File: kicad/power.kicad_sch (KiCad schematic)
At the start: 10 parts, among them Q1 DMN62D0UW-7, U14 TC2117-3.3VDBTR

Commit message: checking shunt footprints
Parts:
- added C53, C54: 220uF 63V, footprints:CHEMI-KG5, symbol Device:C_Polarized
- added C57: 100uF 63V, Capacitor_SMD:CP_Elec_8x10.5, symbol Device:C_Polarized
- C55: renamed from C51; value 470uF 63V -> 100uF 63V; footprint Capacitor_SMD:CP_Elec_16x17.5 -> Capacitor_SMD:CP_Elec_8x10.5
- C56: renamed from C52; value 470uF 63V -> 100uF 63V; footprint Capacitor_SMD:CP_Elec_16x17.5 -> Capacitor_SMD:CP_Elec_8x10.5
- renumbered C53 to C58, C54 to C59, C55 to C60, D2 to D9, Q1 to Q7, R7 to R43, R6 to R44
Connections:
- net GND: now also C53.2, C54.2, C57.2
- net SUPPLY: now also C53.1, C54.1, C57.1
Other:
- moved on the sheet: C55, C56

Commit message: routing gate driver
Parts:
- removed C55, C56, C57: 100uF 63V, Capacitor_SMD:CP_Elec_8x10.5, symbol Device:C_Polarized
- C53, C54: value 220uF 63V -> 470uF 63V; footprint footprints:CHEMI-KG5 -> Capacitor_SMD:CP_Elec_16x17.5
- renumbered C58 to C55, C59 to C56, C60 to C57
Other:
- moved on the sheet: C53

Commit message: gate driver routed to mosfets, working on misc stm32 related components
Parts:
- C53, C54: footprint Capacitor_SMD:CP_Elec_16x17.5 -> footprints:CP_Elec_16x17.5_Panasonic
- U14: footprint SOT-223_3MC_MCH -> footprints:SOT-223_3MC_MCH_Custom
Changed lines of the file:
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@@
 			)
 		)
-		(property "Footprint" "SOT-223_3MC_MCH"
+		(property "Footprint" "footprints:SOT-223_3MC_MCH_Custom"
 			(at 167.64 110.49 0)
 			(effects
@@
 			)
 		)
-		(property "Footprint" "Capacitor_SMD:CP_Elec_16x17.5"
+		(property "Footprint" "footprints:CP_Elec_16x17.5_Panasonic"
 			(at 244.8052 54.61 0)
 			(show_name yes)
@@
 			)
 		)
-		(property "Footprint" "Capacitor_SMD:CP_Elec_16x17.5"
+		(property "Footprint" "footprints:CP_Elec_16x17.5_Panasonic"
 			(at 265.1252 54.61 0)
 			(show_name yes)

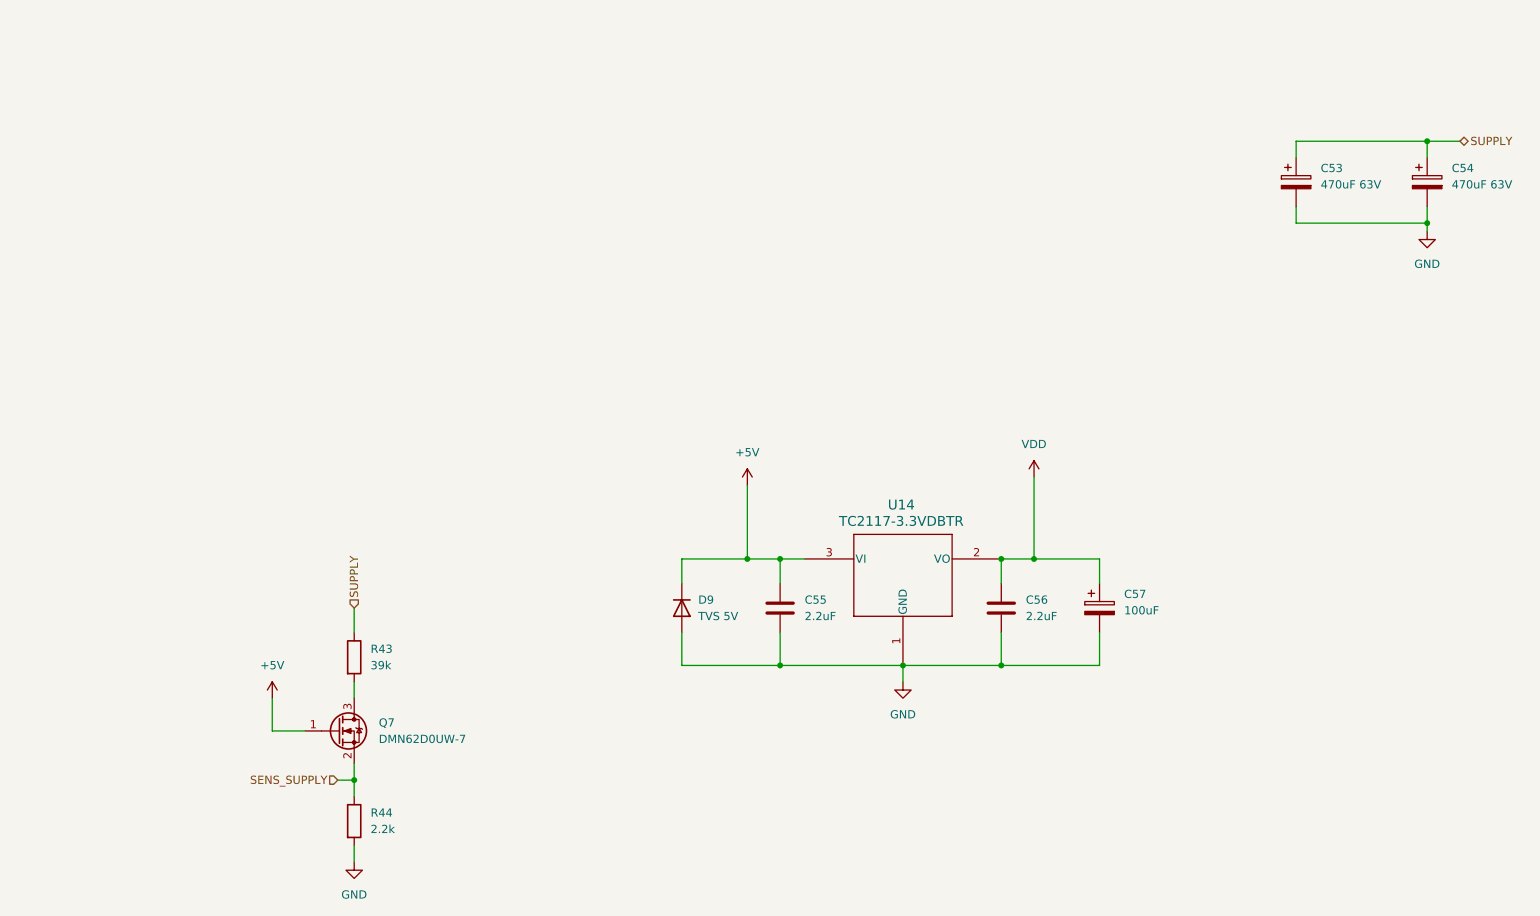
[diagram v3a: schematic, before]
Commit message: finalizing schematic for gate driver
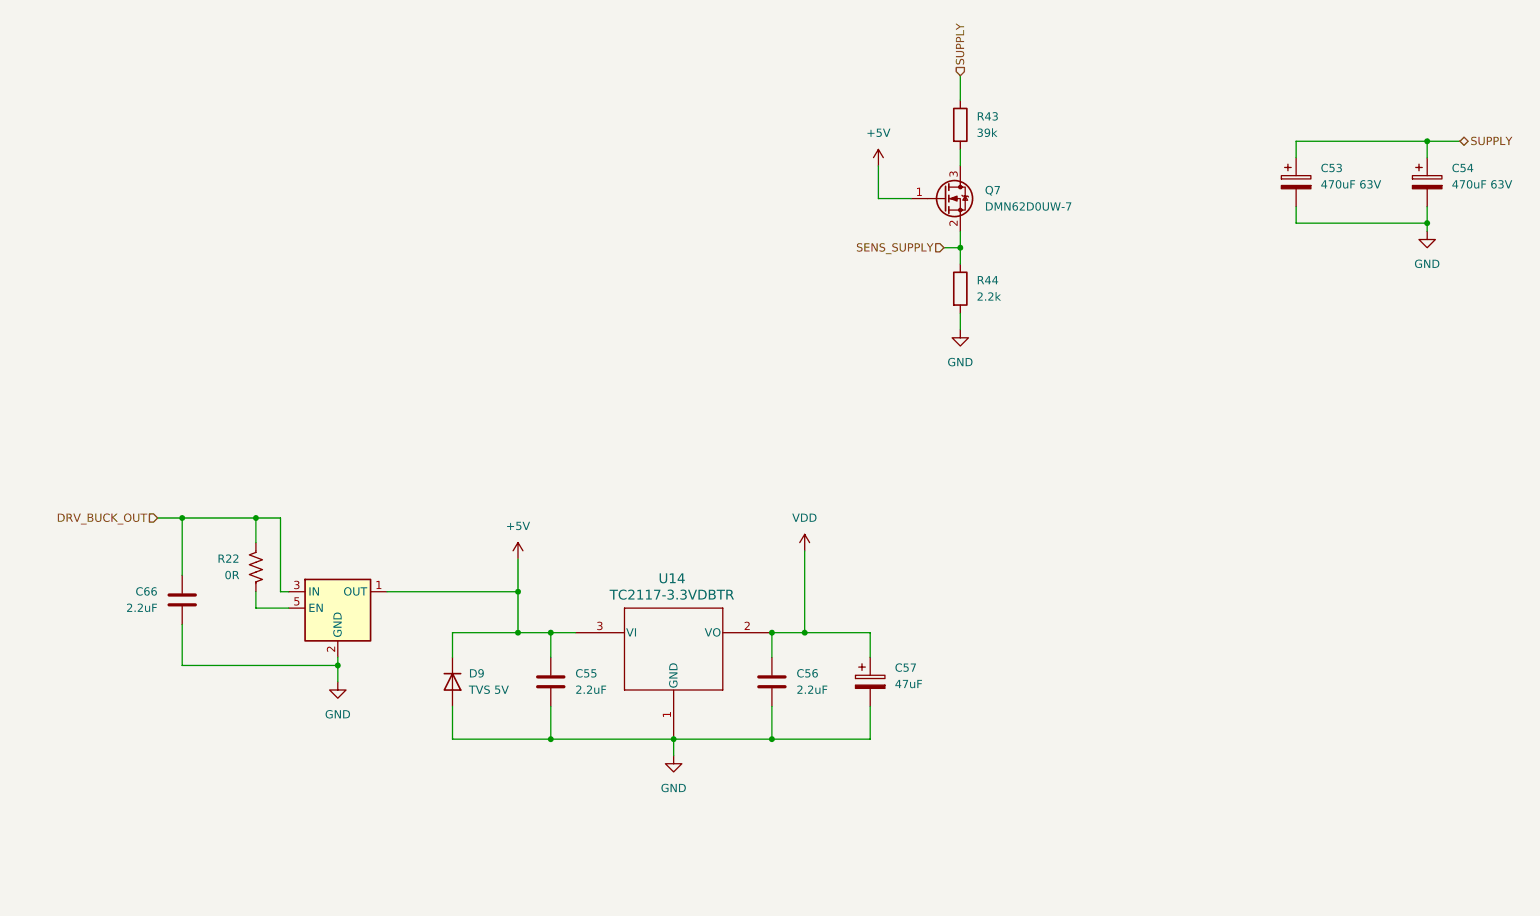
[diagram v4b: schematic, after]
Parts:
- added C66: 2.2uF, Capacitor_SMD:C_0402_1005Metric, symbol Device:C
- added R22: 0R, symbol Device:R_US
- added U17: ~, symbol custom:TPS7B92
- C57: value 100uF -> 47uF
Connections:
- net +5V: now also U17.1 (OUT)
- net GND: now also C66.2, U17.2 (GND)
- new net: R22.2, U17.5 (EN)
- new net DRV_BUCK_OUT: C66.1, R22.1, U17.3 (IN)
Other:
- moved on the sheet: C55, C56, C57, D9, Q7, R43, R44, U14

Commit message: revert to v6.05
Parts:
- R22: footprint (none) -> Resistor_SMD:R_0402_1005Metric
- U17: footprint (none) -> footprints:SOT-23-5-DBV_TEX
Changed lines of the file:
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@@
 	)
 	(hierarchical_label "SUPPLY"
-		(shape input)
+		(shape bidirectional)
 		(at 191.77 34.29 90)
 		(effects
@@
 			)
 		)
-		(property "Footprint" ""
+		(property "Footprint" "Resistor_SMD:R_0402_1005Metric"
 			(at 81.534 110.744 90)
 			(effects
@@
 			)
 		)
-		(property "Footprint" ""
+		(property "Footprint" "footprints:SOT-23-5-DBV_TEX"
 			(at 95.25 115.57 0)
 			(effects

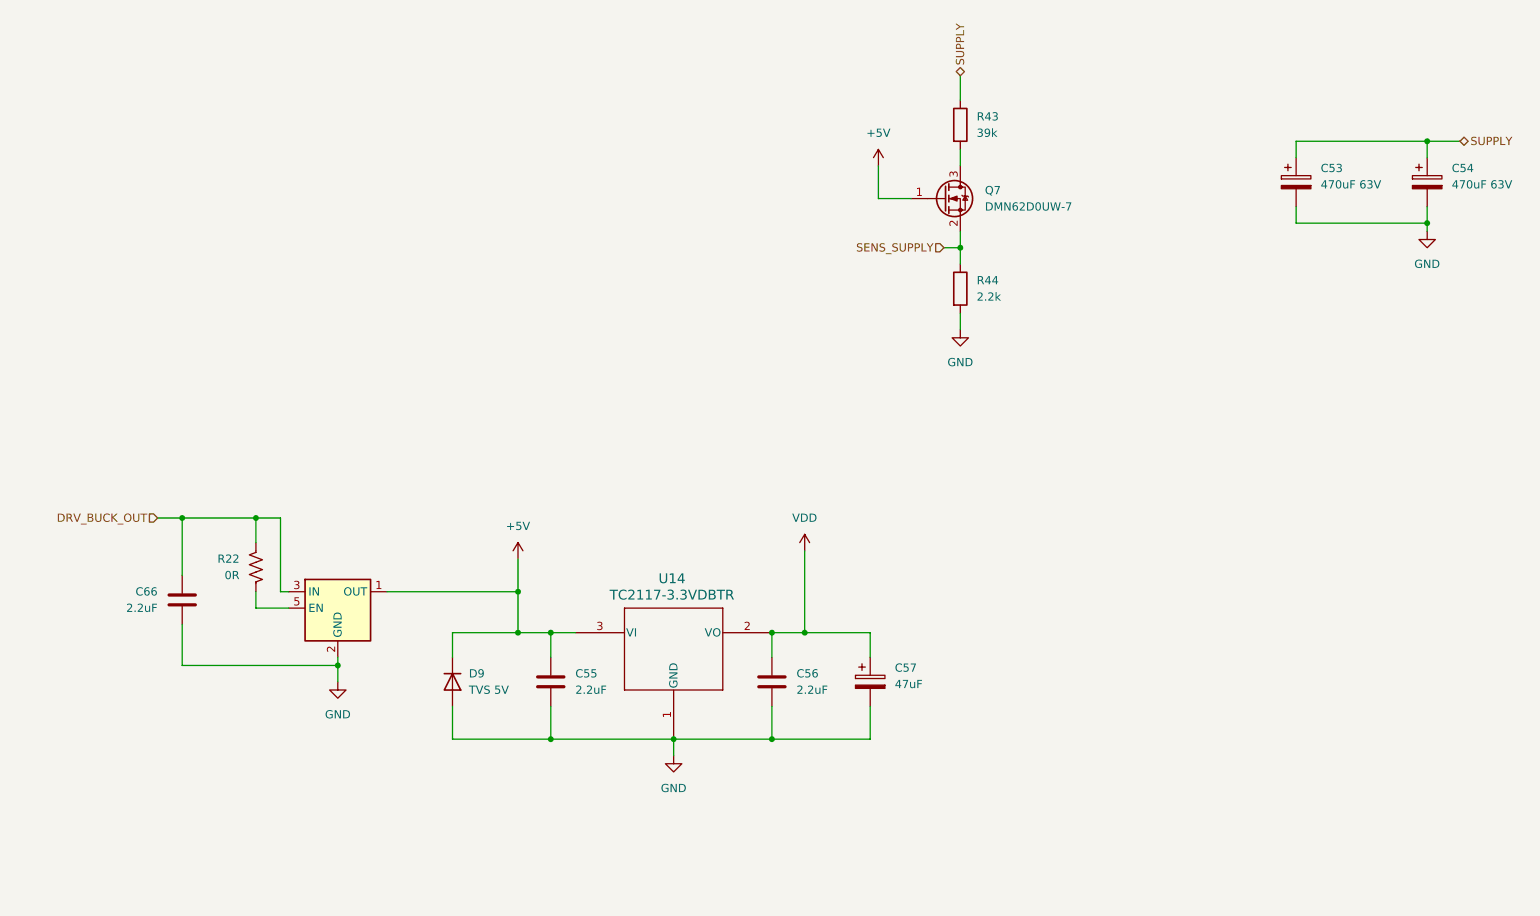
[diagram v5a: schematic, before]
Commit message: gate driver mostly schematic'd and pcb started
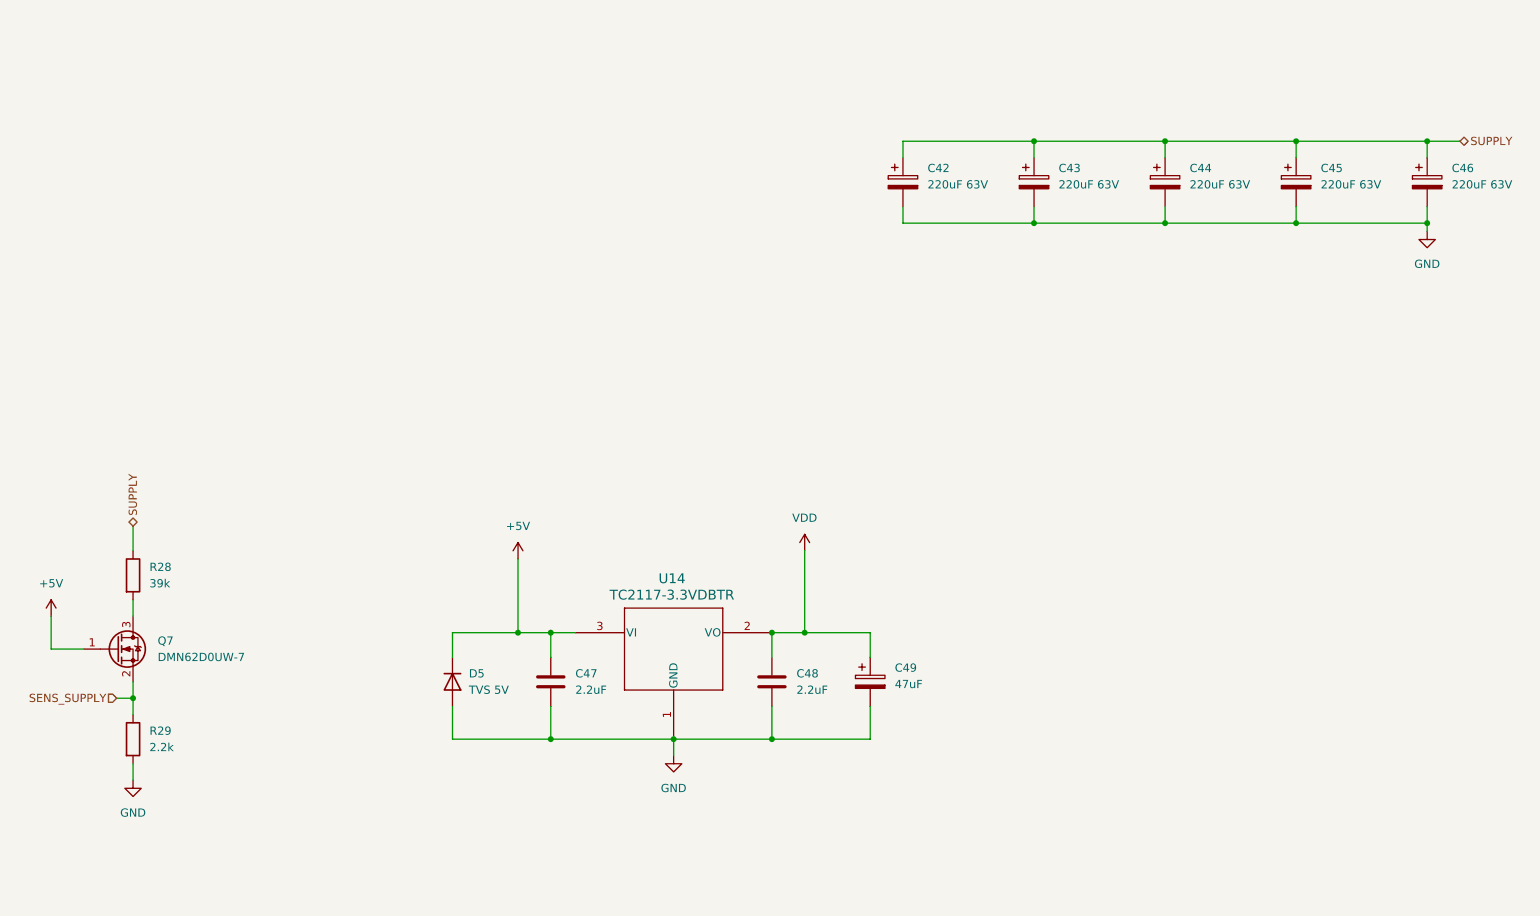
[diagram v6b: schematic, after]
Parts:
- removed C54: 470uF 63V, footprints:CP_Elec_16x17.5_Panasonic, symbol Device:C_Polarized
- removed C66: 2.2uF, Capacitor_SMD:C_0402_1005Metric, symbol Device:C
- removed R22: 0R, Resistor_SMD:R_0402_1005Metric, symbol Device:R_US
- removed U17: ~, footprints:SOT-23-5-DBV_TEX, symbol custom:TPS7B92
- added C42, C43, C44, C46: 220uF 63V, Capacitor_SMD:CP_Elec_10x10, symbol Device:C_Polarized
- C45: renamed from C53; value 470uF 63V -> 220uF 63V; footprint footprints:CP_Elec_16x17.5_Panasonic -> Capacitor_SMD:CP_Elec_10x10
- renumbered C55 to C47, C56 to C48, C57 to C49, D9 to D5, R43 to R28, R44 to R29
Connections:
- net GND: now also C42.2, C43.2, C44.2, C46.2
- net SUPPLY: now also C42.1, C43.1, C44.1, C46.1
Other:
- moved on the sheet: Q7, R28, R29

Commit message: rev3 ordered
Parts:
- removed C49: 47uF, Capacitor_SMD:CP_Elec_5x5.4, symbol Device:C_Polarized
- removed D5: TVS 5V, footprints:SOD-123FL, symbol Device:D
- R43: renamed from R28; symbol Device:R -> Device:R_US
- R44: renamed from R29; symbol Device:R -> Device:R_US
- renumbered C46 to C25, C44 to C26, C43 to C27, C42 to C28, C45 to C53, C47 to C55, C48 to C56
